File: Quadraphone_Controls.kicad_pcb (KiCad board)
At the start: 2 copper layers, 60 x 110 mm, 20 parts, among them J1 Conn_01x10_Female, J10 Pitch_In, J11 Mix_Out, J12 Conn_02x04_Top_Bottom, J13 Conn_01x04_Male, J14 Conn_01x01_Male, J2 Conn_01x10_Female, J3 Conn_01x10_Female, J4 Conn_01x10_Female, J5 PWM_CV, J6 LFO_IN, J7 PWM_CV_In, J8 Synch_Signal_In, J9 Freq_Mod_In, SW1 Synch_Type, SW2 Output_Type

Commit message: Clean up control board
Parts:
- added D1: 3d_Model_Components, Custom_Footprints:3D_Dummy, B.Cu at (80.0, 100.0)
- added D2: 3d_Model_Panel, Custom_Footprints:3D_Dummy, F.Cu at (80.0, 93.0)
- moved J13 0.65 mm to (103.7, 45.3)
- moved J12 0.54 mm to (83.8, 45.2)
- moved J14 0.35 mm to (60.5, 46.3)
- moved J10 0.15 mm to (61.6, 143.5)
- moved J11 0.15 mm to (80.0, 143.5)
- moved J5 0.15 mm to (80.0, 122.5)
- moved J6 0.15 mm to (80.0, 106.5)
- moved J7 0.15 mm to (97.0, 118.5)
- moved J8 0.15 mm to (98.4, 143.5)
- moved J9 0.15 mm to (63.0, 118.5)
- moved PWM_Pot1 0.15 mm to (97.0, 91.5)
- moved SW2 0.15 mm to (66.0, 73.5)
- moved Vibrato_Depth1 0.15 mm to (63.0, 91.5)
- moved Fine_Tune1 0.15 mm to (94.0, 55.0)
- moved Octave_Tune1 0.15 mm to (66.0, 55.0)
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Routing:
- net /TRIANGLE_SW: track 56.9 -> 78.8 mm, vias 0 -> 1
- net /FREQ_MOD1: track 64.6 -> 65.4 mm
- net /V_PER_OCT3: track 157.6 -> 156.8 mm
- net /MIX_OUT2: track 197.9 -> 197.2 mm
- net /MIX_OUT4: track 149.5 -> 148.8 mm
- net /MIX_OUT3: track 172.5 -> 171.9 mm
- net /V_PER_OCT4: track 109.9 -> 109.3 mm
- net /V_PER_OCT1: track 133.8 -> 133.6 mm, vias 1 -> 2
- net GND: vias 44 -> 43
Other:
- board text added: "Quadraphone Controls v2 Mountjoy Modular 2023"
- board text removed: "Quadraphone Controls v2 Mountjoy Modular"

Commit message: Added readme
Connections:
- J11 pad 2: /MIX_OUT3 -> /MIX_OUT2
- J11 pad 3: /MIX_OUT2 -> /MIX_OUT3
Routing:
- net /MIX_OUT3: track 171.9 -> 179.4 mm
- net /V_PER_OCT3: track 156.8 -> 163.8 mm
- net /MIX_OUT2: track 197.2 -> 195.6 mm
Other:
- board text added: "Quadraphone Controls v3 Mountjoy Modular 2023"
- board text removed: "Quadraphone Controls v2 Mountjoy Modular 2023"
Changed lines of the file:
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@@
       (net 8 "/MIX_OUT1") (pintype "passive"))
     (pad "2" thru_hole circle (at -3.13 -7.19) (size 1.5 1.5) (drill 0.9) (layers *.Cu *.Mask)
+      (net 7 "/MIX_OUT2") (pintype "passive"))
+    (pad "3" thru_hole circle (at -1.86 -4.65) (size 1.5 1.5) (drill 0.9) (layers *.Cu *.Mask)
       (net 6 "/MIX_OUT3") (pintype "passive"))
-    (pad "3" thru_hole circle (at -1.86 -4.65) (size 1.5 1.5) (drill 0.9) (layers *.Cu *.Mask)
-      (net 7 "/MIX_OUT2") (pintype "passive"))
     (pad "4" thru_hole circle (at -0.59 -7.19) (size 1.5 1.5) (drill 0.9) (layers *.Cu *.Mask)
       (net 5 "/MIX_OUT4") (pintype "passive"))
@@
     (effects (font (size 1 1) (thickness 0.15)))
   )
-  (gr_text "Quadraphone Controls v2\nMountjoy Modular 2023" (at 81.1 83.3) (layer "F.SilkS")
+  (gr_text "Quadraphone Controls v3\nMountjoy Modular 2023" (at 81.1 83.3) (layer "F.SilkS")
     (effects (font (size 1.5 1.5) (thickness 0.3)))
   )
@@
   (segment (start 52.82 125.08) (end 55.1 122.8) (width 0.3) (layer "B.Cu") (net 5))
   (segment (start 83.1 86.043599) (end 83.1 55) (width 0.3) (layer "B.Cu") (net 5))
-  (segment (start 76.86 136.45) (end 72.8 136.45) (width 0.3) (layer "F.Cu") (net 6))
-  (segment (start 70.25 139) (end 64.82 139) (width 0.3) (layer "F.Cu") (net 6))
   (segment (start 87.567249 62.054499) (end 77.449999 62.054499) (width 0.3) (layer "F.Cu") (net 6))
   (segment (start 97.32 44) (end 79.92 44) (width 0.3) (layer "F.Cu") (net 6))
@@
   (segment (start 99.1 85.6) (end 99.1 73.58725) (width 0.3) (layer "F.Cu") (net 6))
   (segment (start 99.1 73.58725) (end 87.567249 62.054499) (width 0.3) (layer "F.Cu") (net 6))
-  (segment (start 72.8 136.45) (end 70.25 139) (width 0.3) (layer "F.Cu") (net 6))
   (via (at 77.449999 61.904499) (size 0.8) (drill 0.4) (layers "F.Cu" "B.Cu") (net 6))
+  (segment (start 79.25 125.05) (end 76.3 128) (width 0.3) (layer "B.Cu") (net 6))
+  (segment (start 76.3 128) (end 76.3 131.2) (width 0.3) (layer "B.Cu") (net 6))
+  (segment (start 104.45 117.2) (end 99.4 117.2) (width 0.3) (layer "B.Cu") (net 6))
+  (segment (start 78.75 138.85) (end 78.14 138.85) (width 0.3) (layer "B.Cu") (net 6))
+  (segment (start 78.72 45.2) (end 77.449999 46.470001) (width 0.3) (layer "B.Cu") (net 6))
   (segment (start 107.1 119.85) (end 104.45 117.2) (width 0.3) (layer "B.Cu") (net 6))
+  (segment (start 91.55 125.05) (end 79.25 125.05) (width 0.3) (layer "B.Cu") (net 6))
+  (segment (start 76.3 131.2) (end 80.7 135.6) (width 0.3) (layer "B.Cu") (net 6))
+  (segment (start 68.65 138.85) (end 64.82 138.85) (width 0.3) (layer "B.Cu") (net 6))
+  (segment (start 80.7 135.6) (end 80.7 136.9) (width 0.3) (layer "B.Cu") (net 6))
+  (segment (start 76.3 131.2) (end 68.65 138.85) (width 0.3) (layer "B.Cu") (net 6))
+  (segment (start 80.7 136.9) (end 78.75 138.85) (width 0.3) (layer "B.Cu") (net 6))
   (segment (start 99.4 117.2) (end 91.55 125.05) (width 0.3) (layer "B.Cu") (net 6))
-  (segment (start 78.72 45.2) (end 77.449999 46.470001) (width 0.3) (layer "B.Cu") (net 6))
-  (segment (start 91.55 125.05) (end 79.25 125.05) (width 0.3) (layer "B.Cu") (net 6))
-  (segment (start 76.87 127.43) (end 76.87 136.31) (width 0.3) (layer "B.Cu") (net 6))
-  (segment (start 79.25 125.05) (end 76.87 127.43) (width 0.3) (layer "B.Cu") (net 6))
-  (segment (start 104.45 117.2) (end 99.4 117.2) (width 0.3) (layer "B.Cu") (net 6))
   (segment (start 77.449999 46.470001) (end 77.449999 61.904499) (width 0.3) (layer "B.Cu") (net 6))
+  (segment (start 64.3 140.45) (end 71.4 140.45) (width 0.3) (layer "F.Cu") (net 7))
   (segment (start 63.55 139.7) (end 64.3 140.45) (width 0.3) (layer "F.Cu") (net 7))
-  (segment (start 74.25 137.6) (end 76.74 137.6) (width 0.3) (layer "F.Cu") (net 7))
-  (segment (start 76.74 137.6) (end 78.14 139) (width 0.3) (layer "F.Cu") (net 7))
+  (segment (start 71.4 140.45) (end 75.54 136.31) (width 0.3) (layer "F.Cu") (net 7))
   (segment (start 63.55 136.46) (end 63.55 139.7) (width 0.3) (layer "F.Cu") (net 7))
-  (segment (start 71.4 140.45) (end 74.25 137.6) (width 0.3) (layer "F.Cu") (net 7))
-  (segment (start 64.3 140.45) (end 71.4 140.45) (width 0.3) (layer "F.Cu") (net 7))
+  (segment (start 75.54 136.31) (end 76.87 136.31) (width 0.3) (layer "F.Cu") (net 7))
+  (segment (start 75.29 136.31) (end 76.87 136.31) (width 0.3) (layer "B.Cu") (net 7))
   (segment (start 51.2 69.02) (end 52.8 70.62) (width 0.3) (layer "B.Cu") (net 7))
+  (segment (start 50.600499 140.800499) (end 51.4 141.6) (width 0.3) (layer "B.Cu") (net 7))
   (segment (start 80.05 44) (end 53.95 44) (width 0.3) (layer "B.Cu") (net 7))
+  (segment (start 101.16 45.3) (end 99.96 46.5) (width 0.3) (layer "B.Cu") (net 7))
+  (segment (start 52.8 70.62) (end 50.600499 72.819501) (width 0.3) (layer "B.Cu") (net 7))
   (segment (start 50.600499 72.819501) (end 50.600499 140.800499) (width 0.3) (layer "B.Cu") (net 7))
-  (segment (start 51.4 141.6) (end 75.39 141.6) (width 0.3) (layer "B.Cu") (net 7))
-  (segment (start 101.16 45.3) (end 99.96 46.5) (width 0.3) (layer "B.Cu") (net 7))
-  (segment (start 75.39 141.6) (end 78.14 138.85) (width 0.3) (layer "B.Cu") (net 7))
-  (segment (start 52.8 70.62) (end 50.600499 72.819501) (width 0.3) (layer "B.Cu") (net 7))
   (segment (start 53.95 44) (end 51.2 46.75) (width 0.3) (layer "B.Cu") (net 7))
+  (segment (start 51.4 141.6) (end 70 141.6) (width 0.3) (layer "B.Cu") (net 7))
+  (segment (start 70 141.6) (end 75.29 136.31) (width 0.3) (layer "B.Cu") (net 7))
   (segment (start 51.2 46.75) (end 51.2 69.02) (width 0.3) (layer "B.Cu") (net 7))
   (segment (start 99.96 46.5) (end 82.55 46.5) (width 0.3) (layer "B.Cu") (net 7))
   (segment (start 82.55 46.5) (end 80.05 44) (width 0.3) (layer "B.Cu") (net 7))
-  (segment (start 50.600499 140.800499) (end 51.4 141.6) (width 0.3) (layer "B.Cu") (net 7))
   (segment (start 62.28 139) (end 62.28 140.23) (width 0.3) (layer "F.Cu") (net 8))
   (segment (start 109.3 145.25) (end 109.3 70.25) (width 0.3) (layer "F.Cu") (net 8))
@@
   (segment (start 103.35 110.95) (end 79.3 86.9) (width 0.3) (layer "F.Cu") (net 18))
   (via (at 79.3 86.9) (size 0.8) (drill 0.4) (layers "F.Cu" "B.Cu") (net 18))
-  (segment (start 101.95 141.9) (end 104.9 138.95) (width 0.3) (layer "B.Cu") (net 18))
   (segment (start 78.72 47.74) (end 78.72 86.32) (width 0.3) (layer "B.Cu") (net 18))
+  (segment (start 104.9 138.95) (end 101.95 141.9) (width 0.3) (layer "B.Cu") (net 18))
+  (segment (start 74.6 135) (end 69 140.6) (width 0.3) (layer "B.Cu") (net 18))
+  (segment (start 101.95 141.9) (end 78.1 141.9) (width 0.3) (layer "B.Cu") (net 18))
   (segment (start 78.72 86.32) (end 79.3 86.9) (width 0.3) (layer "B.Cu") (net 18))
-  (segment (start 59.74 138.85) (end 61.49 140.6) (width 0.3) (layer "B.Cu") (net 18))
-  (segment (start 71.3 140.6) (end 74.3 137.6) (width 0.3) (layer "B.Cu") (net 18))
-  (segment (start 107 132.7) (end 107.1 132.7) (width 0.3) (layer "B.Cu") (net 18))
-  (segment (start 88.4 141.9) (end 101.95 141.9) (width 0.3) (layer "B.Cu") (net 18))
-  (segment (start 74.3 137.6) (end 84.1 137.6) (width 0.3) (layer "B.Cu") (net 18))
-  (segment (start 104.9 138.95) (end 104.9 134.8) (width 0.3) (layer "B.Cu") (net 18))
-  (segment (start 84.1 137.6) (end 88.4 141.9) (width 0.3) (layer "B.Cu") (net 18))
-  (segment (start 104.9 134.8) (end 107 132.7) (width 0.3) (layer "B.Cu") (net 18))
-  (segment (start 61.49 140.6) (end 71.3 140.6) (width 0.3) (layer "B.Cu") (net 18))
+  (segment (start 76.9 138.3) (end 78.2 137) (width 0.3) (layer "B.Cu") (net 18))
+  (segment (start 107 132.7) (end 104.9 134.8) (width 0.3) (layer "B.Cu") (net 18))
+  (segment (start 78.2 137) (end 78.2 135.6) (width 0.3) (layer "B.Cu") (net 18))
+  (segment (start 76.9 140.7) (end 76.9 138.3) (width 0.3) (layer "B.Cu") (net 18))
+  (segment (start 61.49 140.6) (end 59.74 138.85) (width 0.3) (layer "B.Cu") (net 18))
+  (segment (start 104.9 134.8) (end 104.9 138.95) (width 0.3) (layer "B.Cu") (net 18))
+  (segment (start 78.1 141.9) (end 76.9 140.7) (width 0.3) (layer "B.Cu") (net 18))
+  (segment (start 69 140.6) (end 61.49 140.6) (width 0.3) (layer "B.Cu") (net 18))
+  (segment (start 78.2 135.6) (end 77.6 135) (width 0.3) (layer "B.Cu") (net 18))
+  (segment (start 77.6 135) (end 74.6 135) (width 0.3) (layer "B.Cu") (net 18))
+  (segment (start 107.1 132.7) (end 107 132.7) (width 0.3) (layer "B.Cu") (net 18))
   (segment (start 77 44) (end 77.45 44.45) (width 0.3) (layer "F.Cu") (net 19))
   (segment (start 50.8 85.32) (end 50.8 140.65) (width 0.3) (layer "F.Cu") (net 19))
@@
   (via (at 84.4 131.1) (size 0.8) (drill 0.4) (layers "F.Cu" "B.Cu") (free) (net 24))
   (via (at 56.2 60.8) (size 0.8) (drill 0.4) (layers "F.Cu" "B.Cu") (free) (net 24))
-  (via (at 83.2 142.3) (size 0.8) (drill 0.4) (layers "F.Cu" "B.Cu") (free) (net 24))
+  (via (at 82.939566 142.6495) (size 0.8) (drill 0.4) (layers "F.Cu" "B.Cu") (free) (net 24))
   (via (at 55.8 128.65) (size 0.8) (drill 0.4) (layers "F.Cu" "B.Cu") (free) (net 24))
   (via (at 70.8 130.9) (size 0.8) (drill 0.4) (layers "F.Cu" "B.Cu") (free) (net 24))

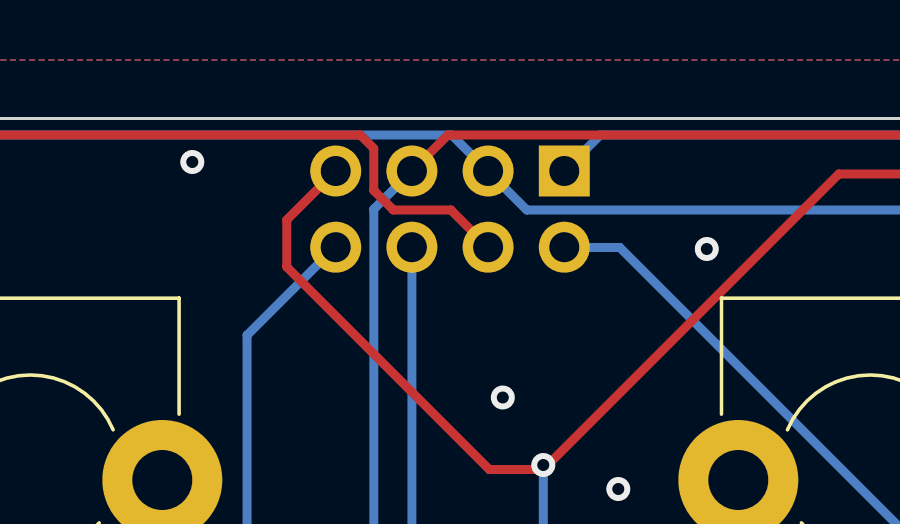
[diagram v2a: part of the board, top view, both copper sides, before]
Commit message: Fixes to footprints on controls board
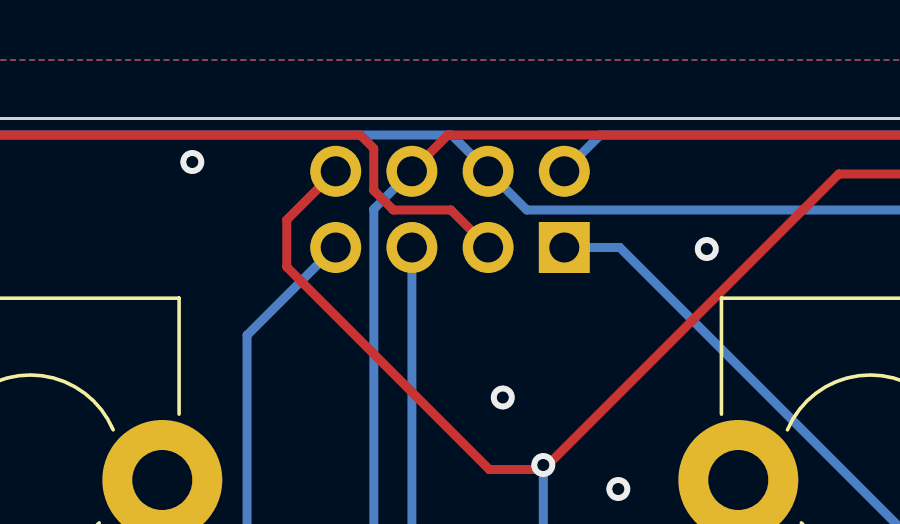
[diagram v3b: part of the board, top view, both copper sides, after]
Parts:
- J12: value Conn_02x04_Top_Bottom -> Conn_02x04_Odd_Even; footprint Connector_PinSocket_2.54mm:PinSocket_2x04_P2.54mm_Vertical -> Connector_PinHeader_2.54mm:PinHeader_2x04_P2.54mm_Vertical
- moved J12 2.55 mm to (83.8, 47.8)
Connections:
- J12 pad 1: /MIX_OUT1 -> /V_PER_OCT1
- J12 pad 2: /MIX_OUT2 -> /MIX_OUT1
- J12 pad 3: /MIX_OUT3 -> /V_PER_OCT2
- J12 pad 4: /MIX_OUT4 -> /MIX_OUT2
- J12 pad 5: /V_PER_OCT1 -> /V_PER_OCT3
- J12 pad 6: /V_PER_OCT2 -> /MIX_OUT3
- J12 pad 7: /V_PER_OCT3 -> /V_PER_OCT4
- J12 pad 8: /V_PER_OCT4 -> /MIX_OUT4
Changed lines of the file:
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@@
     (fp_circle (center -7 -2.4) (end -6.9 -2.4) (layer "F.Fab") (width 0.2) (fill none))
     (pad "1" thru_hole rect (at -4.7 -2.415 90) (size 2.775 2.775) (drill 1.85) (layers *.Cu *.Mask)
-      (net 29 "/PULSE_SW") (pinfunction "Out1") (pintype "bidirectional"))
+      (net 29 "/PULSE_SW") (pinfunction "Out1") (pintype "passive"))
     (pad "2" thru_hole circle (at 0 -2.415 90) (size 2.775 2.775) (drill 1.85) (layers *.Cu *.Mask)
-      (net 27 "+5V") (pinfunction "In") (pintype "bidirectional"))
+      (net 27 "+5V") (pinfunction "In") (pintype "passive"))
     (pad "3" thru_hole circle (at 4.7 -2.415 90) (size 2.775 2.775) (drill 1.85) (layers *.Cu *.Mask)
-      (net 50 "Net-(SW2-Pad3)") (pinfunction "Pin3") (pintype "bidirectional"))
+      (net 50 "Net-(SW2-Pad3)") (pinfunction "Pin3") (pintype "passive"))
     (pad "4" thru_hole circle (at -4.7 2.415 90) (size 2.775 2.775) (drill 1.85) (layers *.Cu *.Mask)
-      (net 35 "/TRIANGLE_SW") (pinfunction "Out2") (pintype "bidirectional"))
+      (net 35 "/TRIANGLE_SW") (pinfunction "Out2") (pintype "passive"))
     (pad "5" thru_hole circle (at 0 2.415 90) (size 2.775 2.775) (drill 1.85) (layers *.Cu *.Mask)
-      (net 50 "Net-(SW2-Pad3)") (pinfunction "Pin5") (pintype "bidirectional"))
+      (net 50 "Net-(SW2-Pad3)") (pinfunction "Pin5") (pintype "passive"))
     (pad "6" thru_hole circle (at 4.7 2.415 90) (size 2.775 2.775) (drill 1.85) (layers *.Cu *.Mask)
-      (net 25 "/SAW_SW") (pinfunction "Out3") (pintype "bidirectional"))
+      (net 25 "/SAW_SW") (pinfunction "Out3") (pintype "passive"))
     (model "${CUSTOM_3D}/100DP3T1B1M2QEH.step"
       (offset (xyz 0 0 0))
@@
     )
   )
-  (footprint "Connector_PinSocket_2.54mm:PinSocket_2x04_P2.54mm_Vertical" (layer "B.Cu")
-    (at 83.8 45.2 90)
-    (descr "Through hole straight socket strip, 2x04, 2.54mm pitch, double cols (from Kicad 4.0.7), script generated")
-    (tags "Through hole socket strip THT 2x04 2.54mm double row")
-    (property "Sheetfile" "Quadraphone_Controls.kicad_sch")
-    (property "Sheetname" "")
-    (attr through_hole)
-    (fp_text reference "J12" (at -1.27 2.77 270) (layer "B.SilkS") hide
-      (effects (font (size 1 1) (thickness 0.15)) (justify mirror))
-    )
-    (fp_text value "Conn_02x04_Top_Bottom" (at -1.27 -10.39 270) (layer "B.Fab")
-      (effects (font (size 1 1) (thickness 0.15)) (justify mirror))
-    )
-    (fp_text user "${REFERENCE}" (at -1.27 -3.81) (layer "B.Fab")
-      (effects (font (size 1 1) (thickness 0.15)) (justify mirror))
-    )
-    (fp_line (start -3.87 1.33) (end -1.27 1.33) (layer "B.SilkS") (width 0.12))
-    (fp_line (start 0 1.33) (end 1.33 1.33) (layer "B.SilkS") (width 0.12))
-    (fp_line (start -1.27 -1.27) (end 1.33 -1.27) (layer "B.SilkS") (width 0.12))
-    (fp_line (start -3.87 -8.95) (end 1.33 -8.95) (layer "B.SilkS") (width 0.12))
-    (fp_line (start -3.87 1.33) (end -3.87 -8.95) (layer "B.SilkS") (width 0.12))
-    (fp_line (start -1.27 1.33) (end -1.27 -1.27) (layer "B.SilkS") (width 0.12))
-    (fp_line (start 1.33 -1.27) (end 1.33 -8.95) (layer "B.SilkS") (width 0.12))
-    (fp_line (start 1.33 1.33) (end 1.33 0) (layer "B.SilkS") (width 0.12))
-    (fp_line (start 1.76 1.8) (end 1.76 -9.4) (layer "B.CrtYd") (width 0.05))
-    (fp_line (start -4.34 1.8) (end 1.76 1.8) (layer "B.CrtYd") (width 0.05))
-    (fp_line (start 1.76 -9.4) (end -4.34 -9.4) (layer "B.CrtYd") (width 0.05))
-    (fp_line (start -4.34 -9.4) (end -4.34 1.8) (layer "B.CrtYd") (width 0.05))
-    (fp_line (start -3.81 -8.89) (end -3.81 1.27) (layer "B.Fab") (width 0.1))
-    (fp_line (start 1.27 -8.89) (end -3.81 -8.89) (layer "B.Fab") (width 0.1))
-    (fp_line (start 1.27 0.27) (end 1.27 -8.89) (layer "B.Fab") (width 0.1))
-    (fp_line (start -3.81 1.27) (end 0.27 1.27) (layer "B.Fab") (width 0.1))
-    (fp_line (start 0.27 1.27) (end 1.27 0.27) (layer "B.Fab") (width 0.1))
+  (footprint "Connector_PinHeader_2.54mm:PinHeader_2x04_P2.54mm_Vertical" (layer "B.Cu")
+    (at 83.8 47.75 90)
+    (descr "Through hole straight pin header, 2x04, 2.54mm pitch, double rows")
+    (tags "Through hole pin header THT 2x04 2.54mm double row")
+    (property "Sheetfile" "Quadraphone_Controls.kicad_sch")
+    (property "Sheetname" "")
+    (attr through_hole)
+    (fp_text reference "J12" (at 1.27 2.33 270) (layer "B.SilkS") hide
+      (effects (font (size 1 1) (thickness 0.15)) (justify mirror))
+    )
+    (fp_text value "Conn_02x04_Odd_Even" (at 1.27 -9.95 270) (layer "B.Fab")
+      (effects (font (size 1 1) (thickness 0.15)) (justify mirror))
+    )
+    (fp_text user "${REFERENCE}" (at 1.27 -3.81) (layer "B.Fab")
+      (effects (font (size 1 1) (thickness 0.15)) (justify mirror))
+    )
+    (fp_line (start -1.33 -1.27) (end 1.27 -1.27) (layer "B.SilkS") (width 0.12))
+    (fp_line (start -1.33 -1.27) (end -1.33 -8.95) (layer "B.SilkS") (width 0.12))
+    (fp_line (start -1.33 -8.95) (end 3.87 -8.95) (layer "B.SilkS") (width 0.12))
+    (fp_line (start 3.87 1.33) (end 3.87 -8.95) (layer "B.SilkS") (width 0.12))
+    (fp_line (start -1.33 0) (end -1.33 1.33) (layer "B.SilkS") (width 0.12))
+    (fp_line (start 1.27 -1.27) (end 1.27 1.33) (layer "B.SilkS") (width 0.12))
+    (fp_line (start -1.33 1.33) (end 0 1.33) (layer "B.SilkS") (width 0.12))
+    (fp_line (start 1.27 1.33) (end 3.87 1.33) (layer "B.SilkS") (width 0.12))
+    (fp_line (start 4.35 1.8) (end -1.8 1.8) (layer "B.CrtYd") (width 0.05))
+    (fp_line (start -1.8 -9.4) (end 4.35 -9.4) (layer "B.CrtYd") (width 0.05))
+    (fp_line (start 4.35 -9.4) (end 4.35 1.8) (layer "B.CrtYd") (width 0.05))
+    (fp_line (start -1.8 1.8) (end -1.8 -9.4) (layer "B.CrtYd") (width 0.05))
+    (fp_line (start 3.81 1.27) (end 3.81 -8.89) (layer "B.Fab") (width 0.1))
+    (fp_line (start -1.27 -8.89) (end -1.27 0) (layer "B.Fab") (width 0.1))
+    (fp_line (start -1.27 0) (end 0 1.27) (layer "B.Fab") (width 0.1))
+    (fp_line (start 0 1.27) (end 3.81 1.27) (layer "B.Fab") (width 0.1))
+    (fp_line (start 3.81 -8.89) (end -1.27 -8.89) (layer "B.Fab") (width 0.1))
     (pad "1" thru_hole rect (at 0 0 90) (size 1.7 1.7) (drill 1) (layers *.Cu *.Mask)
-      (net 8 "/MIX_OUT1") (pinfunction "Pin_1") (pintype "passive"))
-    (pad "2" thru_hole oval (at 0 -2.54 90) (size 1.7 1.7) (drill 1) (layers *.Cu *.Mask)
-      (net 7 "/MIX_OUT2") (pinfunction "Pin_2") (pintype "passive"))
-    (pad "3" thru_hole oval (at 0 -5.08 90) (size 1.7 1.7) (drill 1) (layers *.Cu *.Mask)
-      (net 6 "/MIX_OUT3") (pinfunction "Pin_3") (pintype "passive"))
-    (pad "4" thru_hole oval (at 0 -7.62 90) (size 1.7 1.7) (drill 1) (layers *.Cu *.Mask)
-      (net 5 "/MIX_OUT4") (pinfunction "Pin_4") (pintype "passive"))
-    (pad "5" thru_hole oval (at -2.54 0 90) (size 1.7 1.7) (drill 1) (layers *.Cu *.Mask)
-      (net 20 "/V_PER_OCT1") (pinfunction "Pin_5") (pintype "passive"))
-    (pad "6" thru_hole oval (at -2.54 -2.54 90) (size 1.7 1.7) (drill 1) (layers *.Cu *.Mask)
-      (net 19 "/V_PER_OCT2") (pinfunction "Pin_6") (pintype "passive"))
-    (pad "7" thru_hole oval (at -2.54 -5.08 90) (size 1.7 1.7) (drill 1) (layers *.Cu *.Mask)
-      (net 18 "/V_PER_OCT3") (pinfunction "Pin_7") (pintype "passive"))
-    (pad "8" thru_hole oval (at -2.54 -7.62 90) (size 1.7 1.7) (drill 1) (layers *.Cu *.Mask)
-      (net 17 "/V_PER_OCT4") (pinfunction "Pin_8") (pintype "passive"))
-    (model "${KICAD6_3DMODEL_DIR}/Connector_PinHeader_2.54mm.3dshapes/PinHeader_2x04_P2.54mm_Vertical.step"
-      (offset (xyz -2.5 0 0))
-      (scale (xyz 1 1 1))
-      (rotate (xyz 0 0 0))
+      (net 20 "/V_PER_OCT1") (pinfunction "Pin_1") (pintype "passive"))
+    (pad "2" thru_hole oval (at 2.54 0 90) (size 1.7 1.7) (drill 1) (layers *.Cu *.Mask)
+      (net 8 "/MIX_OUT1") (pinfunction "Pin_2") (pintype "passive"))
+    (pad "3" thru_hole oval (at 0 -2.54 90) (size 1.7 1.7) (drill 1) (layers *.Cu *.Mask)
+      (net 19 "/V_PER_OCT2") (pinfunction "Pin_3") (pintype "passive"))
+    (pad "4" thru_hole oval (at 2.54 -2.54 90) (size 1.7 1.7) (drill 1) (layers *.Cu *.Mask)
+      (net 7 "/MIX_OUT2") (pinfunction "Pin_4") (pintype "passive"))
+    (pad "5" thru_hole oval (at 0 -5.08 90) (size 1.7 1.7) (drill 1) (layers *.Cu *.Mask)
+      (net 18 "/V_PER_OCT3") (pinfunction "Pin_5") (pintype "passive"))
+    (pad "6" thru_hole oval (at 2.54 -5.08 90) (size 1.7 1.7) (drill 1) (layers *.Cu *.Mask)
+      (net 6 "/MIX_OUT3") (pinfunction "Pin_6") (pintype "passive"))
+    (pad "7" thru_hole oval (at 0 -7.62 90) (size 1.7 1.7) (drill 1) (layers *.Cu *.Mask)
+      (net 17 "/V_PER_OCT4") (pinfunction "Pin_7") (pintype "passive"))
+    (pad "8" thru_hole oval (at 2.54 -7.62 90) (size 1.7 1.7) (drill 1) (layers *.Cu *.Mask)
+      (net 5 "/MIX_OUT4") (pinfunction "Pin_8") (pintype "passive"))
+    (model "${KICAD6_3DMODEL_DIR}/Connector_PinHeader_2.54mm.3dshapes/PinHeader_2x04_P2.54mm_Vertical.wrl"
+      (offset (xyz 0 0 0))
+      (scale (xyz 1 1 1))
+      (rotate (xyz 0 0 0))
